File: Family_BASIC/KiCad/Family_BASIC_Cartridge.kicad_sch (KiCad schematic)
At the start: 18 parts, among them IC1 Working RAM (62256), IC2 PRG ROM (27256), IC3 74HCT20, IC4 CHR ROM (27C64), SW1 BACKUP SW, SW2 RAM BANK SW

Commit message: PCB layout started
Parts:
- added BT2: 1.5V, Battery:BatteryHolder_Multicomp_BC-2001_1x2032, symbol Device:Battery_Cell
- BT1: value 3V -> 1.5V; footprint (none) -> Battery:BatteryHolder_Multicomp_BC-2001_1x2032
- D1, D2: value D -> 1N4148; footprint (none) -> Diode_THT:D_DO-35_SOD27_P7.62mm_Horizontal
- R1, R2, R3: footprint (none) -> Resistor_THT:R_Axial_DIN0207_L6.3mm_D2.5mm_P7.62mm_Horizontal
- SW1: footprint (none) -> Button_Switch_THT:SW_E-Switch_EG1224_SPDT_Angled
- SW2: footprint (none) -> Button_Switch_THT:SW_DIP_SPSTx02_Slide_9.78x7.26mm_W7.62mm_P2.54mm
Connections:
- net GND: now also BT2.2 (-); no longer BT1.2 (-)
- net SWA_{13}: now also SW2.3; no longer SW2.4
- net SWA_{14}: now also SW2.4; no longer SW2.3
- new net: BT1.2 (-), BT2.1 (+)
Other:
- moved on the sheet: SW2
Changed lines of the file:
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@@
 	)
 	(junction
-		(at 205.74 123.19)
-		(diameter 0)
-		(color 0 0 0 0)
-	)
-	(junction
 		(at 166.37 104.14)
 		(diameter 0)
@@
 	)
 	(junction
-		(at 168.91 123.19)
+		(at 73.66 193.04)
 		(diameter 0)
 		(color 0 0 0 0)
 	)
 	(junction
-		(at 73.66 193.04)
+		(at 113.03 186.69)
 		(diameter 0)
 		(color 0 0 0 0)
 	)
 	(junction
-		(at 113.03 186.69)
+		(at 167.64 130.81)
 		(diameter 0)
 		(color 0 0 0 0)
@@
 	)
 	(junction
+		(at 205.74 130.81)
+		(diameter 0)
+		(color 0 0 0 0)
+	)
+	(junction
 		(at 101.6 130.81)
 		(diameter 0)
@@
 	)
 	(junction
+		(at 167.64 123.19)
+		(diameter 0)
+		(color 0 0 0 0)
+	)
+	(junction
 		(at 60.96 167.64)
 		(diameter 0)
@@
 	(wire
 		(pts
-			(xy 205.74 123.19) (xy 243.84 123.19)
-		)
-		(stroke
-			(width 0)
-			(type default)
-		)
-	)
-	(wire
-		(pts
 			(xy 125.73 53.34) (xy 134.62 53.34)
 		)
@@
 	(wire
 		(pts
+			(xy 167.64 130.81) (xy 205.74 130.81)
+		)
+		(stroke
+			(width 0)
+			(type default)
+		)
+	)
+	(wire
+		(pts
 			(xy 22.86 99.06) (xy 34.29 99.06)
 		)
@@
 		)
 	)
-	(bus
+	(wire
 		(pts
-			(xy 20.32 104.14) (xy 20.32 107.95)
+			(xy 167.64 123.19) (xy 168.91 123.19)
 		)
 		(stroke
@@
 		)
 	)
-	(wire
+	(bus
 		(pts
-			(xy 190.5 36.83) (xy 190.5 40.64)
+			(xy 20.32 104.14) (xy 20.32 107.95)
 		)
 		(stroke
@@
 	(wire
 		(pts
-			(xy 243.84 106.68) (xy 243.84 123.19)
+			(xy 190.5 36.83) (xy 190.5 40.64)
 		)
 		(stroke
@@
 	(wire
 		(pts
-			(xy 64.77 80.01) (xy 64.77 82.55)
+			(xy 243.84 106.68) (xy 243.84 130.81)
 		)
 		(stroke
@@
 	(wire
 		(pts
-			(xy 168.91 130.81) (xy 168.91 123.19)
+			(xy 64.77 80.01) (xy 64.77 82.55)
 		)
 		(stroke
@@
 	(wire
 		(pts
+			(xy 205.74 130.81) (xy 243.84 130.81)
+		)
+		(stroke
+			(width 0)
+			(type default)
+		)
+	)
+	(wire
+		(pts
 			(xy 60.96 167.64) (xy 60.96 175.26)
 		)
@@
 	(wire
 		(pts
-			(xy 144.78 130.81) (xy 168.91 130.81)
+			(xy 205.74 127) (xy 205.74 130.81)
+		)
+		(stroke
+			(width 0)
+			(type default)
+		)
+	)
+	(wire
+		(pts
+			(xy 144.78 130.81) (xy 167.64 130.81)
 		)
 		(stroke
@@
 	(wire
 		(pts
-			(xy 166.37 123.19) (xy 168.91 123.19)
+			(xy 166.37 123.19) (xy 167.64 123.19)
 		)
 		(stroke
@@
 	(wire
 		(pts
+			(xy 167.64 130.81) (xy 167.64 123.19)
+		)
+		(stroke
+			(width 0)
+			(type default)
+		)
+	)
+	(wire
+		(pts
 			(xy 125.73 55.88) (xy 134.62 55.88)
 		)
@@
 		)
 	)
-	(wire
-		(pts
-			(xy 168.91 123.19) (xy 205.74 123.19)
-		)
-		(stroke
-			(width 0)
-			(type default)
-		)
-	)
 	(bus
 		(pts
@@
 	(wire
 		(pts
-			(xy 205.74 123.19) (xy 205.74 119.38)
-		)
-		(stroke
-			(width 0)
-			(type default)
-		)
-	)
-	(wire
-		(pts
 			(xy 129.54 83.82) (xy 134.62 83.82)
 		)
@@
 	)
 	(label "GND"
-		(at 184.15 123.19 0)
+		(at 184.15 130.81 0)
 		(effects
 			(font
@@
 	)
 	(label "GND"
-		(at 50.8 130.81 0)
+		(at 53.34 130.81 0)
 		(effects
 			(font
@@
 	)
 	(label "GND"
-		(at 101.6 96.52 0)
+		(at 101.6 101.6 0)
 		(effects
 			(font
@@
 	)
 	(label "GND"
-		(at 144.78 93.98 0)
+		(at 144.78 101.6 0)
 		(effects
 			(font
@@
 			)
 		)
-		(property "Footprint" ""
+		(property "Footprint" "Resistor_THT:R_Axial_DIN0207_L6.3mm_D2.5mm_P7.62mm_Horizontal"
 			(at 177.8 105.918 90)
 			(effects
@@
 			)
 		)
-		(property "Footprint" ""
+		(property "Footprint" "Resistor_THT:R_Axial_DIN0207_L6.3mm_D2.5mm_P7.62mm_Horizontal"
 			(at 177.8 100.838 90)
 			(effects
@@
 	(symbol
 		(lib_id "Switch:SW_DIP_x02")
-		(at 168.91 115.57 90)
+		(at 166.37 115.57 270)
+		(mirror x)
 		(unit 1)
 		(exclude_from_sim no)
@@
 		(on_board yes)
 		(dnp no)
-		(fields_autoplaced yes)
 		(property "Reference" "SW2"
-			(at 172.72 114.2999 90)
+			(at 162.56 114.2999 90)
 			(effects
 				(font
@@
 		)
 		(property "Value" "RAM BANK SW"
-			(at 172.72 116.8399 90)
+			(at 162.56 116.8399 90)
 			(effects
 				(font
@@
 			)
 		)
-		(property "Footprint" ""
-			(at 168.91 115.57 0)
+		(property "Footprint" "Button_Switch_THT:SW_DIP_SPSTx02_Slide_9.78x7.26mm_W7.62mm_P2.54mm"
+			(at 166.37 115.57 0)
 			(effects
 				(font
@@
 		)
 		(property "Datasheet" "~"
-			(at 168.91 115.57 0)
+			(at 166.37 115.57 0)
 			(effects
 				(font
@@
 		)
 		(property "Description" "2x DIP Switch, Single Pole Single Throw (SPST) switch, small symbol"
-			(at 168.91 115.57 0)
+			(at 166.37 115.57 0)
 			(effects
 				(font
@@
 		)
 		(instances
-			(project ""
+			(project "Family_BASIC_Cartridge"
 				(path "/d387318e-3d77-436c-8e35-eead167b1d94"
 					(reference "SW2")
@@
 			)
 		)
-		(property "Value" "D"
+		(property "Value" "1N4148"
 			(at 208.28 109.2199 90)
 			(effects
@@
 			)
 		)
-		(property "Footprint" ""
+		(property "Footprint" "Diode_THT:D_DO-35_SOD27_P7.62mm_Horizontal"
 			(at 205.74 107.95 0)
 			(effects
@@
 			)
 		)
-		(property "Value" "3V"
+		(property "Value" "1.5V"
 			(at 209.55 116.2684 0)
 			(effects
@@
 			)
 		)
-		(property "Footprint" ""
+		(property "Footprint" "Battery:BatteryHolder_Multicomp_BC-2001_1x2032"
 			(at 205.74 115.316 90)
 			(effects
@@
 		(fields_autoplaced yes)
 		(property "Reference" "D2"
-			(at 198.12 107.95 0)
+			(at 198.12 95.25 0)
 			(effects
 				(font
@@
 			)
 		)
-		(property "Value" "D"
-			(at 198.12 105.41 0)
+		(property "Value" "1N4148"
+			(at 198.12 97.79 0)
 			(effects
 				(font
@@
 			)
 		)
-		(property "Footprint" ""
+		(property "Footprint" "Diode_THT:D_DO-35_SOD27_P7.62mm_Horizontal"
 			(at 198.12 101.6 0)
 			(effects
@@
 			)
 		)
-		(property "Footprint" ""
+		(property "Footprint" "Resistor_THT:R_Axial_DIN0207_L6.3mm_D2.5mm_P7.62mm_Horizontal"
 			(at 211.328 90.17 90)
 			(effects
@@
 			)
 		)
-		(property "Footprint" ""
+		(property "Footprint" "Button_Switch_THT:SW_E-Switch_EG1224_SPDT_Angled"
 			(at 232.41 86.36 0)
 			(effects
@@
 				)
 			)
+		)
+	)
+	(symbol
+		(lib_id "Device:Battery_Cell")
+		(at 205.74 124.46 0)
+		(unit 1)
+		(exclude_from_sim no)
+		(in_bom yes)
+		(on_board yes)
+		(dnp no)
+		(fields_autoplaced yes)
+		(property "Reference" "BT2"
+			(at 209.55 121.3484 0)
+			(effects
+				(font
+					(size 1.27 1.27)
+				)
+				(justify left)
+			)
+		)
+		(property "Value" "1.5V"
+			(at 209.55 123.8884 0)
+			(effects
+				(font
+					(size 1.27 1.27)
+				)
+				(justify left)
+			)
+		)
+		(property "Footprint" "Battery:BatteryHolder_Multicomp_BC-2001_1x2032"
+			(at 205.74 122.936 90)
+			(effects
+				(font
+					(size 1.27 1.27)
+				)
+				(hide yes)
+			)
+		)
+		(property "Datasheet" "~"
+			(at 205.74 122.936 90)
+			(effects
+				(font
+					(size 1.27 1.27)
+				)
+				(hide yes)
+			)
+		)
+		(property "Description" "Single-cell battery"
+			(at 205.74 124.46 0)
+			(effects
+				(font
+					(size 1.27 1.27)
+				)
+				(hide yes)
+			)
+		)
+		(pin "2"
+		)
+		(pin "1"
+		)
+		(instances
+			(project "Family_BASIC_Cartridge"
+				(path "/d387318e-3d77-436c-8e35-eead167b1d94"
+					(reference "BT2")
+					(unit 1)
+				)
+			)

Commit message: PCB design continues
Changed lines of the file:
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@@
+		)
+	)
+	(text_box "Family BASIC V3 is hard-coded for a maximum of 4KB:\n\nbasicProgram .eq $6006 ; The start of the BASIC program in memory\nbgGetRam     .eq $6c00 {addr/1024} ; region to save bg data with BGGET\nmemoryTop    .eq $6fff ; What FRETOP is set to by default\n\nPossible to increase to 8KB by patching those constants?\n\nbgGetRam     .eq $7c00 {addr/1024} ; region to save bg data with BGGET\nmemoryTop    .eq $7fff ; What FRETOP is set to by default"
+		(exclude_from_sim no)
+		(at 184.15 139.7 0)
+		(size 91.44 24.13)
+		(margins 0.9525 0.9525 0.9525 0.9525)
+		(stroke
+			(width 0)
+			(type solid)
+		)
+		(fill
+			(type none)
+		)
+		(effects
+			(font
+				(size 1.27 1.27)
+			)
+			(justify left top)
 		)
 	)

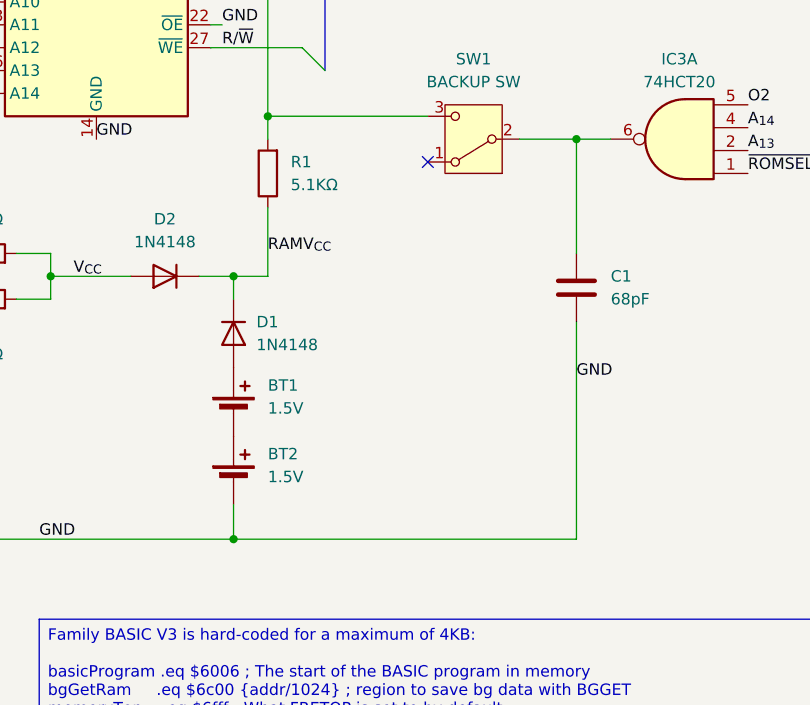
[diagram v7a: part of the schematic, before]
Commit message: Initial PCB layout completed
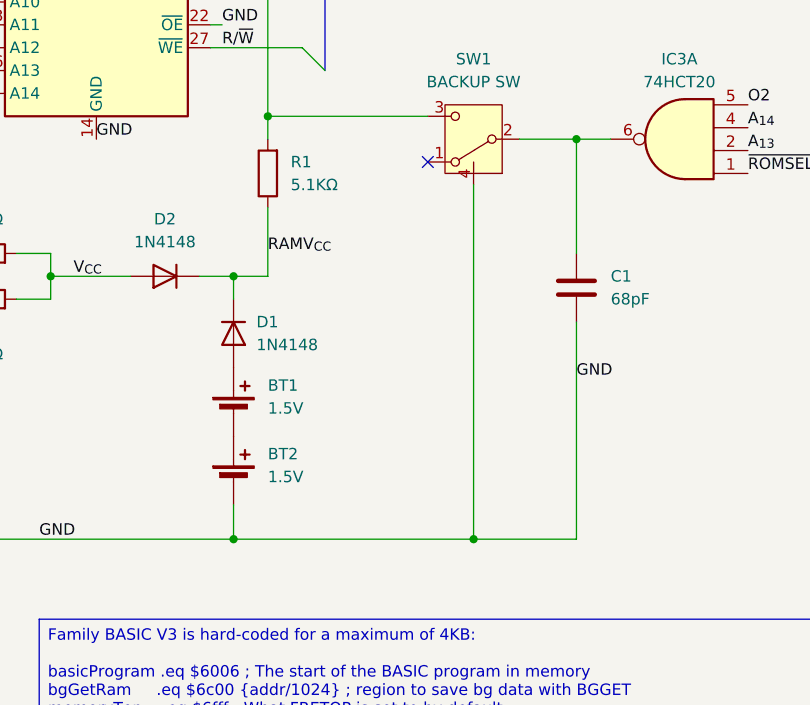
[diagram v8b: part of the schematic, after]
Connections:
- net GND: now also SW1.4 (GND)
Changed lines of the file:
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@@
 	)
 	(junction
+		(at 232.41 130.81)
+		(diameter 0)
+		(color 0 0 0 0)
+	)
+	(junction
 		(at 73.66 193.04)
 		(diameter 0)
@@
 	(wire
 		(pts
-			(xy 205.74 130.81) (xy 243.84 130.81)
+			(xy 205.74 130.81) (xy 232.41 130.81)
 		)
 		(stroke
@@
 	(wire
 		(pts
+			(xy 232.41 91.44) (xy 232.41 130.81)
+		)
+		(stroke
+			(width 0)
+			(type default)
+		)
+	)
+	(wire
+		(pts
 			(xy 154.94 63.5) (xy 163.83 63.5)
 		)
@@
 	(wire
 		(pts
+			(xy 232.41 130.81) (xy 243.84 130.81)
+		)
+		(stroke
+			(width 0)
+			(type default)
+		)
+	)
+	(wire
+		(pts
 			(xy 125.73 45.72) (xy 134.62 45.72)
 		)
@@
 		(pin "2"
 		)
+		(pin "4"
+		)
 		(instances
